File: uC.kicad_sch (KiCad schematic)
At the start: 49 parts, among them J401 Conn_02x05_Counter_Clockwise, J402 Conn_02x05_Counter_Clockwise, J403 Conn_02x08_Counter_Clockwise, SW401 SW_Push, SW402 SW_Push, U401 STM32F103RGT6, U402 BLUENRG-M2SA, Y401 16MHz, Y402 32.768KHz

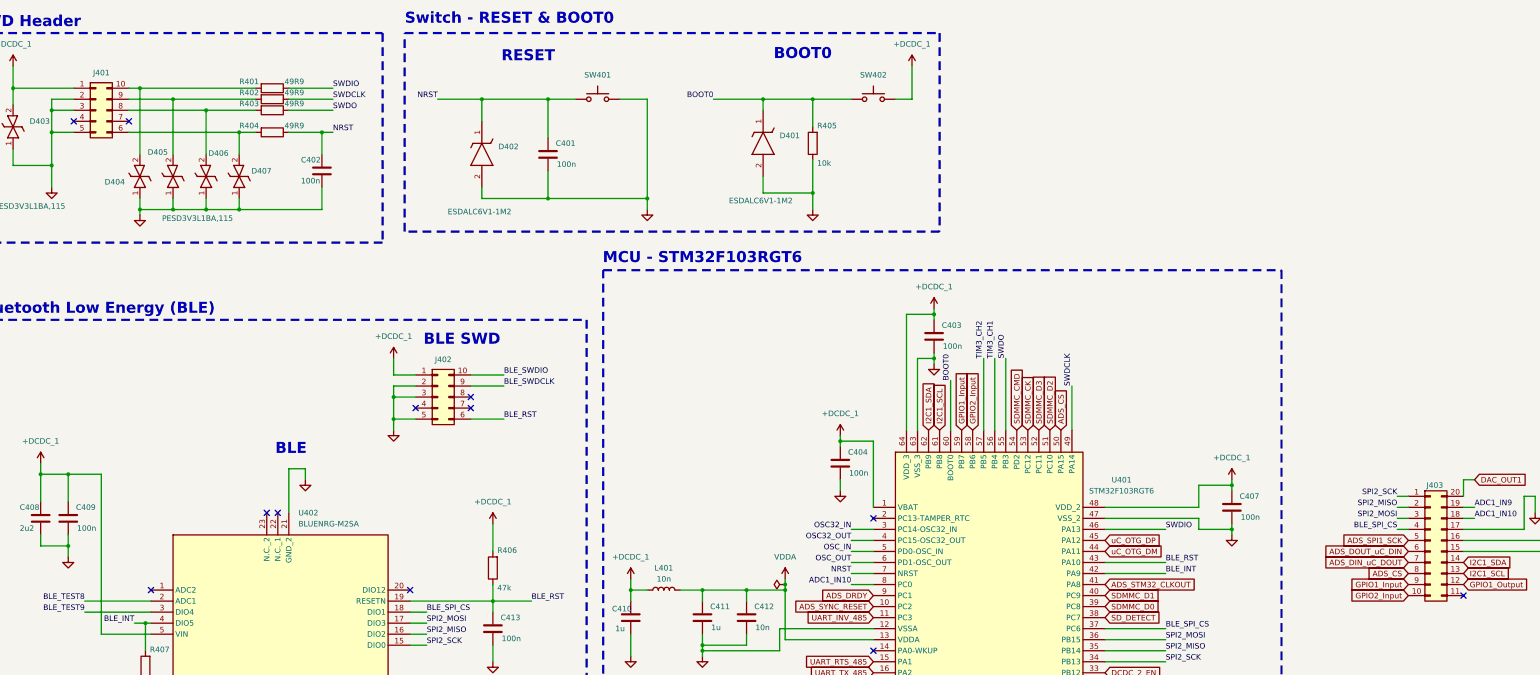
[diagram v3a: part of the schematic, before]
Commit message: pcb layout init
1. Pulled all items from schematics
2. Set board stackup and constraints
3. Create polygon pours for power and ground
4. Created isolated ground and power
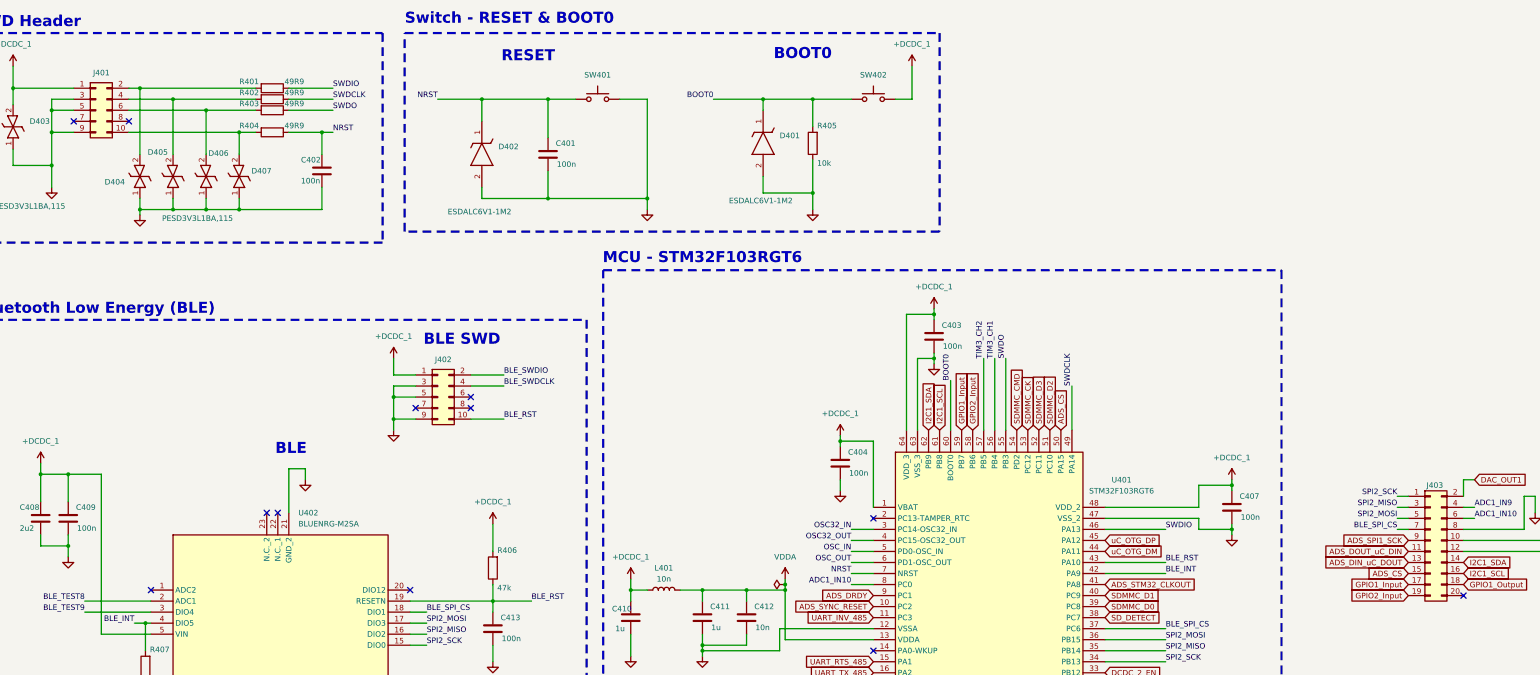
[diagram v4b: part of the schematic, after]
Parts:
- J401, J402: symbol Connector_Generic:Conn_02x05_Counter_Clockwise -> Connector_Generic:Conn_02x05_Odd_Even
- J403: symbol Connector_Generic:Conn_02x10_Counter_Clockwise -> Connector_Generic:Conn_02x10_Odd_Even
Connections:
- net +DCDC_1: now also J403.10 (Pin_10); no longer J403.16 (Pin_16)
- net +DCDC_2: now also J403.12 (Pin_12); no longer J403.15 (Pin_15)
- net ADC1_IN10: now also J403.6 (Pin_6); no longer J403.18 (Pin_18)
- net ADC1_IN9: now also J403.4 (Pin_4); no longer J403.19 (Pin_19)
- net ADS_CS: now also J403.15 (Pin_15); no longer J403.8 (Pin_8)
- net ADS_DIN_uC_DOUT: now also J403.13 (Pin_13); no longer J403.7 (Pin_7)
- net ADS_DOUT_uC_DIN: now also J403.11 (Pin_11); no longer J403.6 (Pin_6)
- net ADS_SPI1_SCK: now also J403.9 (Pin_9); no longer J403.5 (Pin_5)
- net BLE_RST: now also J402.10 (Pin_10); no longer J402.6 (Pin_6)
- net BLE_SPI_CS: now also J403.7 (Pin_7); no longer J403.4 (Pin_4)
- net BLE_SWDCLK: now also J402.4 (Pin_4); no longer J402.9 (Pin_9)
- net BLE_SWDIO: now also J402.2 (Pin_2); no longer J402.10 (Pin_10)
- net DAC_OUT1: now also J403.2 (Pin_2); no longer J403.20 (Pin_20)
- net GND: now also J401.9 (Pin_9), J402.9 (Pin_9), J403.8 (Pin_8); no longer J401.2 (Pin_2), J402.2 (Pin_2), J403.17 (Pin_17)
- net GPIO1_Input: now also J403.17 (Pin_17); no longer J403.9 (Pin_9)
- net GPIO1_Output: now also J403.18 (Pin_18); no longer J403.12 (Pin_12)
- net GPIO2_Input: now also J403.19 (Pin_19); no longer J403.10 (Pin_10)
- net I2C1_SCL: now also J403.16 (Pin_16); no longer J403.13 (Pin_13)
- net SPI2_MISO: now also J403.3 (Pin_3); no longer J403.2 (Pin_2)
- net SPI2_MOSI: now also J403.5 (Pin_5); no longer J403.3 (Pin_3)
- net at D404.2 (K2), R401.2: now also J401.2 (Pin_2); no longer J401.10 (Pin_10)
- net at D406.2 (K2), R403.2: now also J401.6 (Pin_6); no longer J401.8 (Pin_8)
- net at D405.2 (K2), R402.2: now also J401.4 (Pin_4); no longer J401.9 (Pin_9)
- net at D407.2 (K2), R404.2: now also J401.10 (Pin_10); no longer J401.6 (Pin_6)
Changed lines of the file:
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@@
 	)
 	(symbol
-		(lib_id "Connector_Generic:Conn_02x10_Counter_Clockwise")
+		(lib_id "Connector_Generic:Conn_02x10_Odd_Even")
 		(at 353.06 140.97 0)
 		(unit 1)
@@
 			)
 		)
-		(property "Datasheet" "https://www.mouser.com/datasheet/2/181/M20_972-1218753.pdf"
+		(property "Datasheet" "~"
 			(at 353.06 140.97 0)
 			(effects
@@
 			)
 		)
-		(property "Description" "Generic connector, double row, 02x10, counter clockwise pin numbering scheme (similar to DIP package numbering), script generated (kicad-library-utils/schlib/autogen/connector/)"
+		(property "Description" "Generic connector, double row, 02x10, odd/even pin numbering scheme (row 1 odd numbers, row 2 even numbers), script generated (kicad-library-utils/schlib/autogen/connector/)"
 			(at 353.06 140.97 0)
 			(effects
@@
 	)
 	(symbol
-		(lib_id "Connector_Generic:Conn_02x05_Counter_Clockwise")
+		(lib_id "Connector_Generic:Conn_02x05_Odd_Even")
 		(at 45.72 41.91 0)
 		(unit 1)
@@
 			)
 		)
-		(property "Datasheet" "https://www.we-online.com/components/products/datasheet/62701021621.pdf"
+		(property "Datasheet" "~"
 			(at 45.72 41.91 0)
 			(effects
@@
 			)
 		)
-		(property "Description" "Generic connector, double row, 02x05, counter clockwise pin numbering scheme (similar to DIP package numbering), script generated (kicad-library-utils/schlib/autogen/connector/)"
+		(property "Description" "Generic connector, double row, 02x05, odd/even pin numbering scheme (row 1 odd numbers, row 2 even numbers), script generated (kicad-library-utils/schlib/autogen/connector/)"
 			(at 45.72 41.91 0)
 			(effects
@@
 	)
 	(symbol
-		(lib_id "Connector_Generic:Conn_02x05_Counter_Clockwise")
+		(lib_id "Connector_Generic:Conn_02x05_Odd_Even")
 		(at 124.46 107.95 0)
 		(unit 1)
@@
 			)
 		)
-		(property "Datasheet" "https://www.we-online.com/components/products/datasheet/62701021621.pdf"
+		(property "Datasheet" "~"
 			(at 124.46 107.95 0)
 			(effects
@@
 			)
 		)
-		(property "Description" "Generic connector, double row, 02x05, counter clockwise pin numbering scheme (similar to DIP package numbering), script generated (kicad-library-utils/schlib/autogen/connector/)"
+		(property "Description" "Generic connector, double row, 02x05, odd/even pin numbering scheme (row 1 odd numbers, row 2 even numbers), script generated (kicad-library-utils/schlib/autogen/connector/)"
 			(at 124.46 107.95 0)
 			(effects

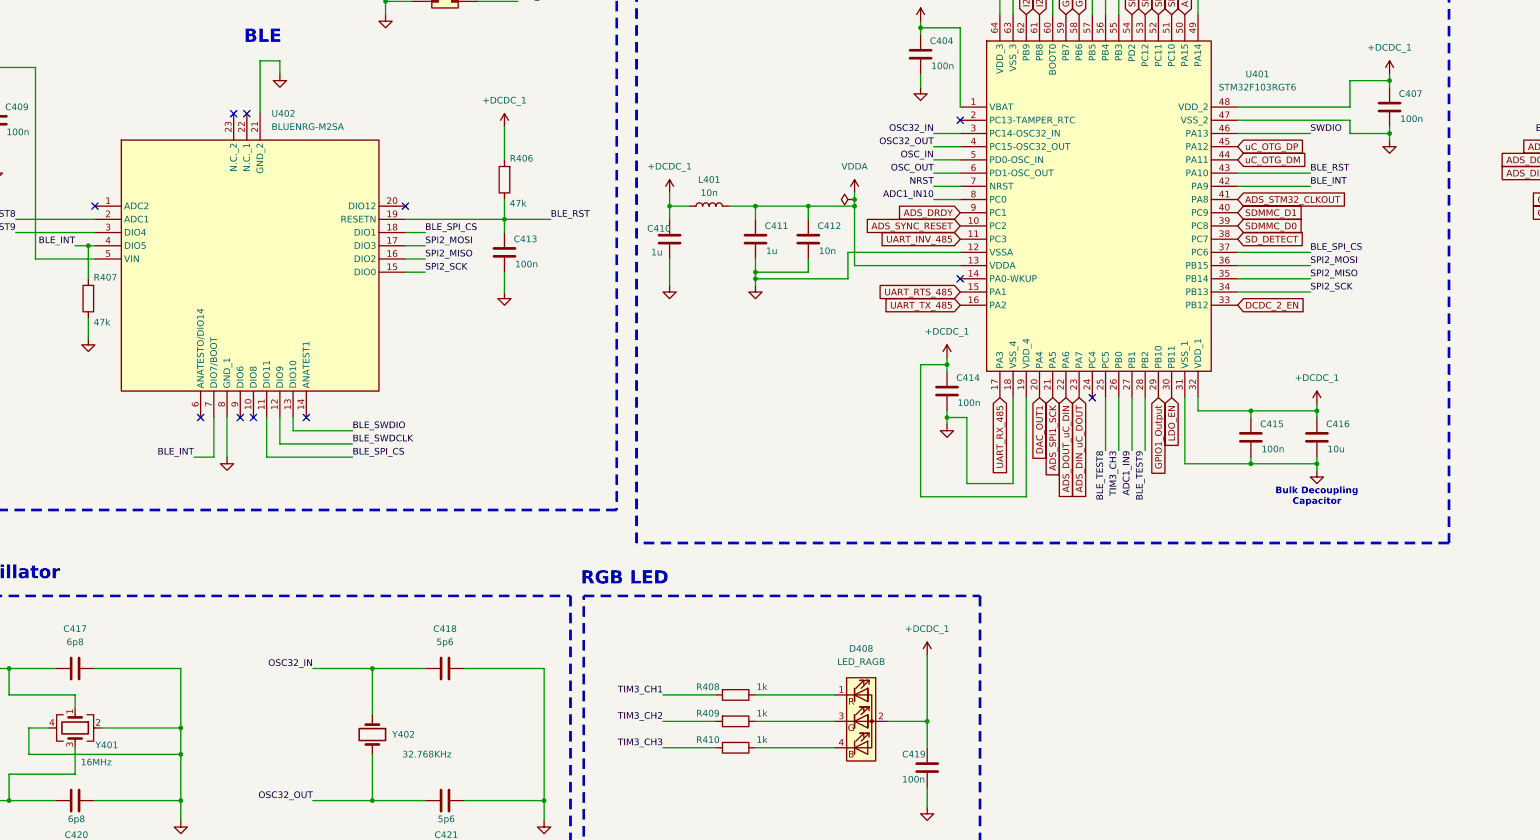
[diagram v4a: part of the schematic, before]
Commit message: routing for blueNRG complete
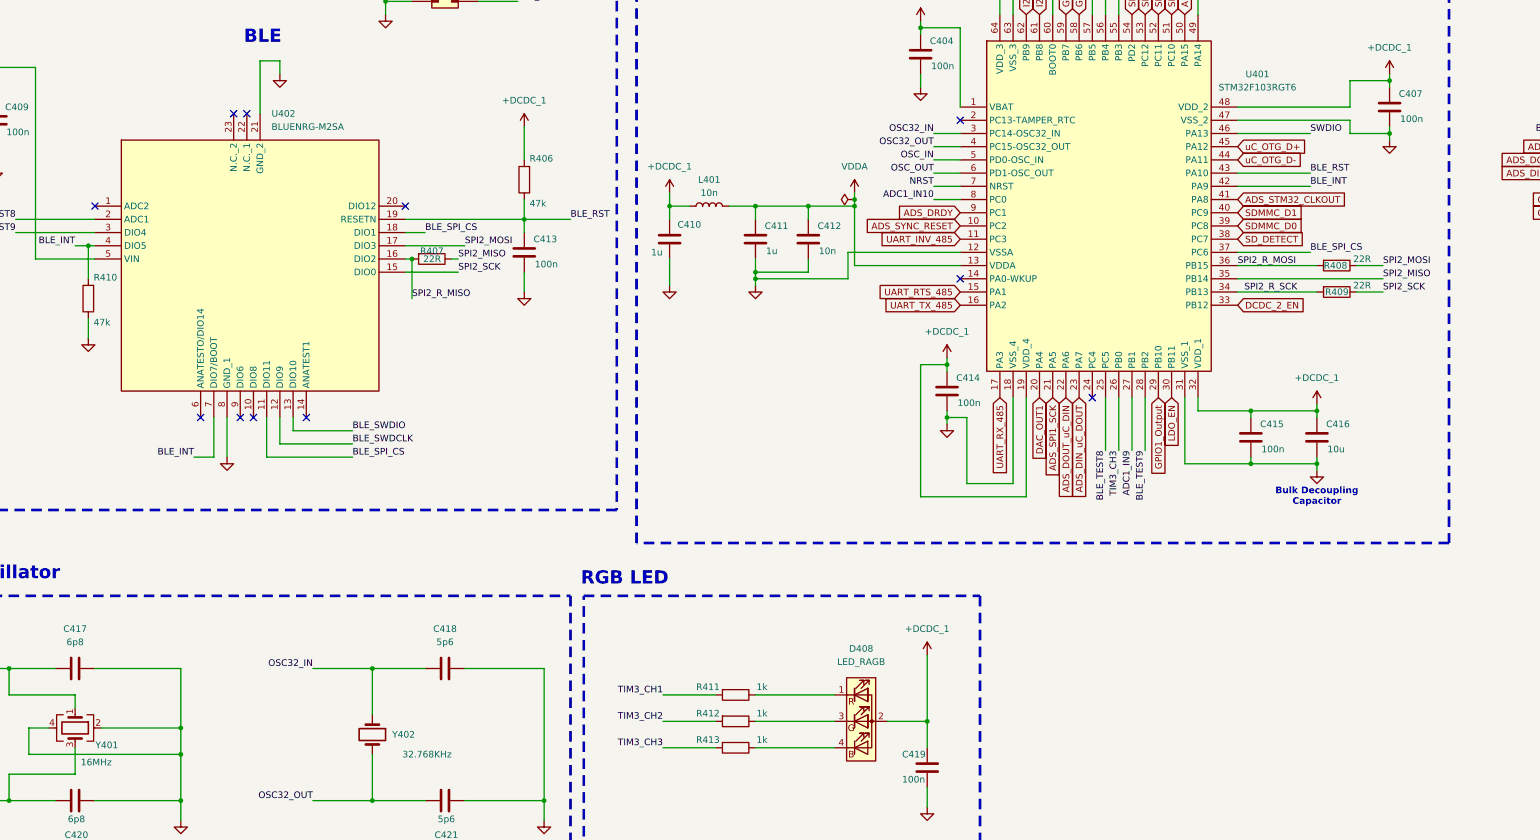
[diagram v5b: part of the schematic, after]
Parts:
- added R407, R408, R409: 22R, Resistor_SMD:R_0603_1608Metric, symbol Device:R
- renumbered R407 to R410, R408 to R411, R409 to R412, R410 to R413
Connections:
- net SPI2_MISO: now also R407.1; no longer U402.16 (DIO2)
- net SPI2_MOSI: now also R408.1; no longer U401.36 (PB15)
- net SPI2_SCK: now also R409.1; no longer U401.34 (PB13)
- net uC_OTG_DM renamed uC_OTG_D-
- net uC_OTG_DP renamed uC_OTG_D+
- new net SPI2_R_MISO: R407.2, U402.16 (DIO2)
- new net SPI2_R_MOSI: R408.2, U401.36 (PB15)
- new net SPI2_R_SCK: R409.2, U401.34 (PB13)
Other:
- moved on the sheet: C413, R406

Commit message: all connections complete
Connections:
- net ADS_DRDY: now also J403.20 (Pin_20)
- no-connect marks 17 -> 16
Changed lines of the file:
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@@
 	)
 	(no_connect
-		(at 360.68 153.67)
-	)
-	(no_connect
 		(at 78.74 193.04)
 	)
@@
 				(hide yes)
 			)
+		)
+	)
+	(global_label "ADS_DRDY"
+		(shape input)
+		(at 360.68 153.67 0)
+		(fields_autoplaced yes)
+		(effects
+			(font
+				(size 1.27 1.27)
+			)
+			(justify left)
+		)
+		(property "Intersheetrefs" "${INTERSHEET_REFS}"
+			(at 373.0995 153.67 0)
+			(effects
+				(font
+					(size 1.27 1.27)
+				)
+				(justify left)
+				(hide yes)
+			)

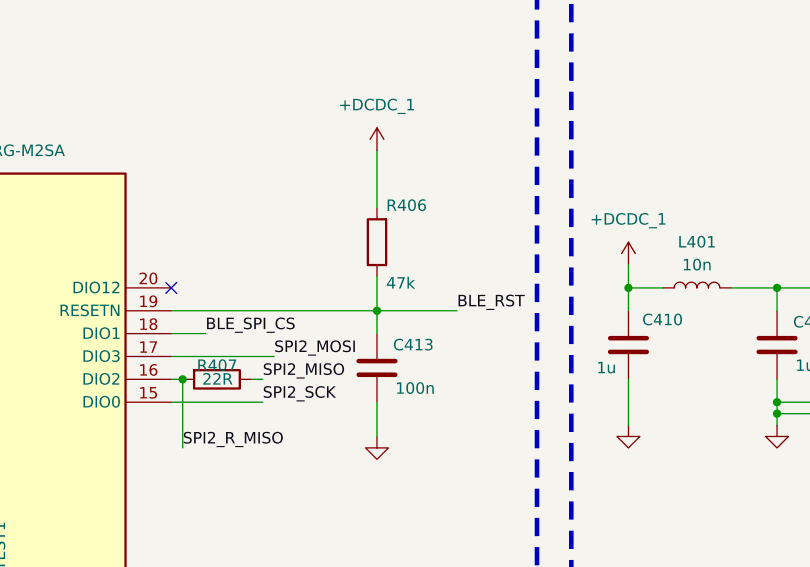
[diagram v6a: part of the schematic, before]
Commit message: change in opAmp config
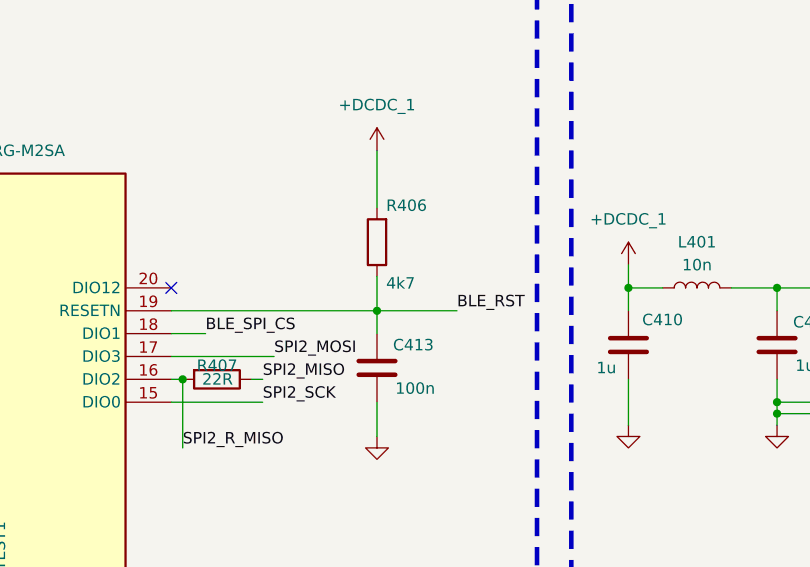
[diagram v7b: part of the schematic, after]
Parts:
- R406: value 47k -> 4k7; Distributor_Link https://www.mouser.com/ProductDetail/Vishay-Dale/CRCW060347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 -> https://www.mouser.com/ProductDetail/YAGEO/SR0603FR-7T4K7L?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; Manufacturer_Name Vishay/Dale -> YAGEO; Manufacturer_Part_Number CRCW060347K0FKEAHP -> SR0603FR-7T4K7L
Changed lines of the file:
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@@
 			)
 		)
-		(property "Value" "47k"
+		(property "Value" "4k7"
 			(at 141.986 151.892 0)
 			(effects
@@
 			)
 		)
-		(property "Datasheet" "https://www.vishay.com/doc?20043"
+		(property "Datasheet" "https://www.mouser.com/datasheet/2/447/PYu_SR_20105_RoHS_L_12-3461462.pdf"
 			(at 140.97 147.32 0)
 			(effects
@@
 			)
 		)
-		(property "Distributor_Link" "https://www.mouser.com/ProductDetail/Vishay-Dale/CRCW060347K0FKEAHP?qs=k2%2FDWSARqgGdf8xU6XXKnw%3D%3D"
+		(property "Distributor_Link" "https://www.mouser.com/ProductDetail/YAGEO/SR0603FR-7T4K7L?qs=1mbolxNpo8e2BYIAXFrBnQ%3D%3D"
 			(at 140.97 147.32 0)
 			(effects
@@
 			)
 		)
-		(property "Manufacturer_Name" "Vishay/Dale"
+		(property "Manufacturer_Name" "YAGEO"
 			(at 140.97 147.32 0)
 			(effects
@@
 			)
 		)
-		(property "Manufacturer_Part_Number" "CRCW060347K0FKEAHP"
+		(property "Manufacturer_Part_Number" "SR0603FR-7T4K7L"
 			(at 140.97 147.32 0)
 			(effects

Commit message: finalized design v1.0.0
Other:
- note added: "[2] MCU"
- company: (none) -> Manufacturing Innovation Network Laboratory (MINLab)
- title: (none) -> Energy Monitoring System
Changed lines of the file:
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@@
 	(generator_version "8.0")
 	(paper "A3")
+	(title_block
+		(title "Energy Monitoring System")
+		(rev "v1.0.0")
+		(company "Manufacturing Innovation Network Laboratory (MINLab)")
+		(comment 1 "Developed by Vignesh Selvaraj")
+	)
 	(junction
 		(at 222.25 182.88)
@@
 				(bold yes)
 			)
+		)
+	)
+	(text "[2] MCU\n"
+		(exclude_from_sim no)
+		(at 359.918 27.178 0)
+		(effects
+			(font
+				(size 11.43 11.43)
+				(thickness 2.286)
+				(bold yes)
+			)
